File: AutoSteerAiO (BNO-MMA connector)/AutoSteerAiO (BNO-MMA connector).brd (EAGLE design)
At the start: 114.3 x 99.1 mm, 88 parts, among them J4 CONNECTOR 1x5 PINS, K4 CB1A-P-12V, T1 BC547, U1 VX7805-1000

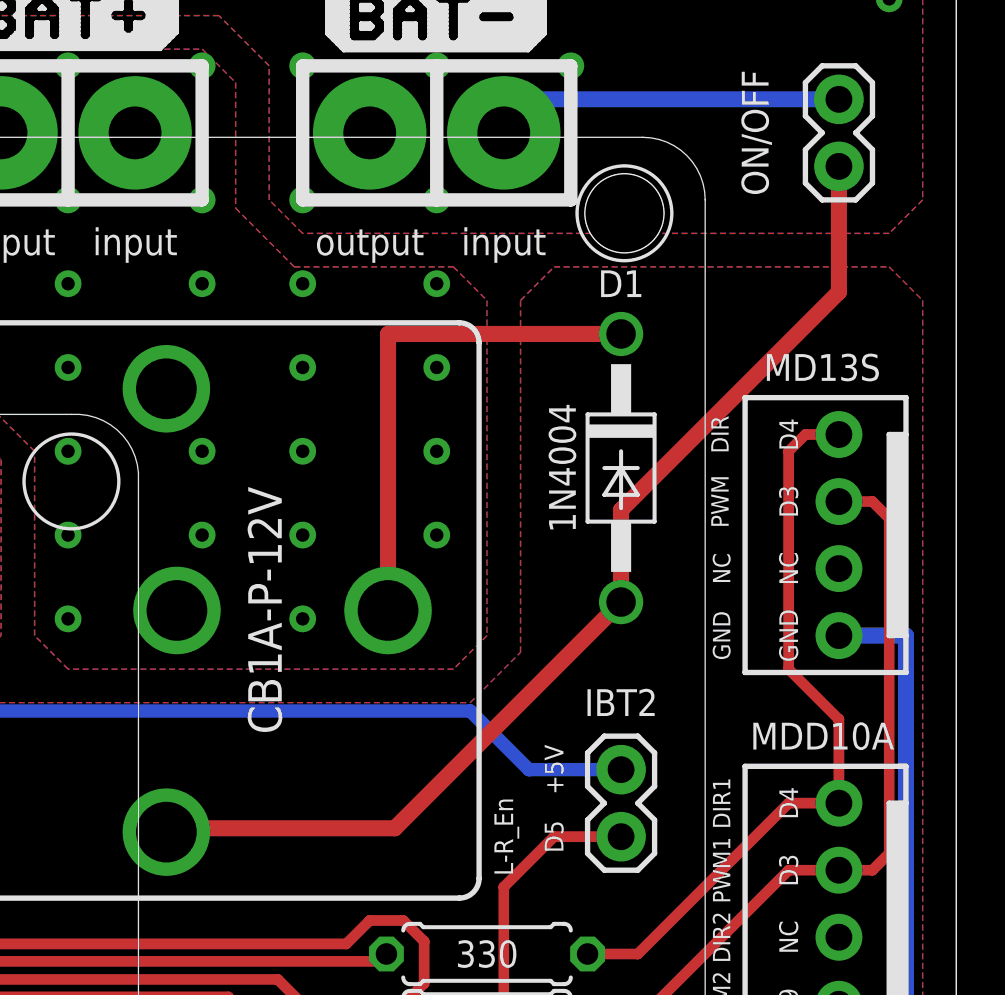
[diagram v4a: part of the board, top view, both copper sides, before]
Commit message: Add files via upload
Added diode D6 to protect from reverse polarity
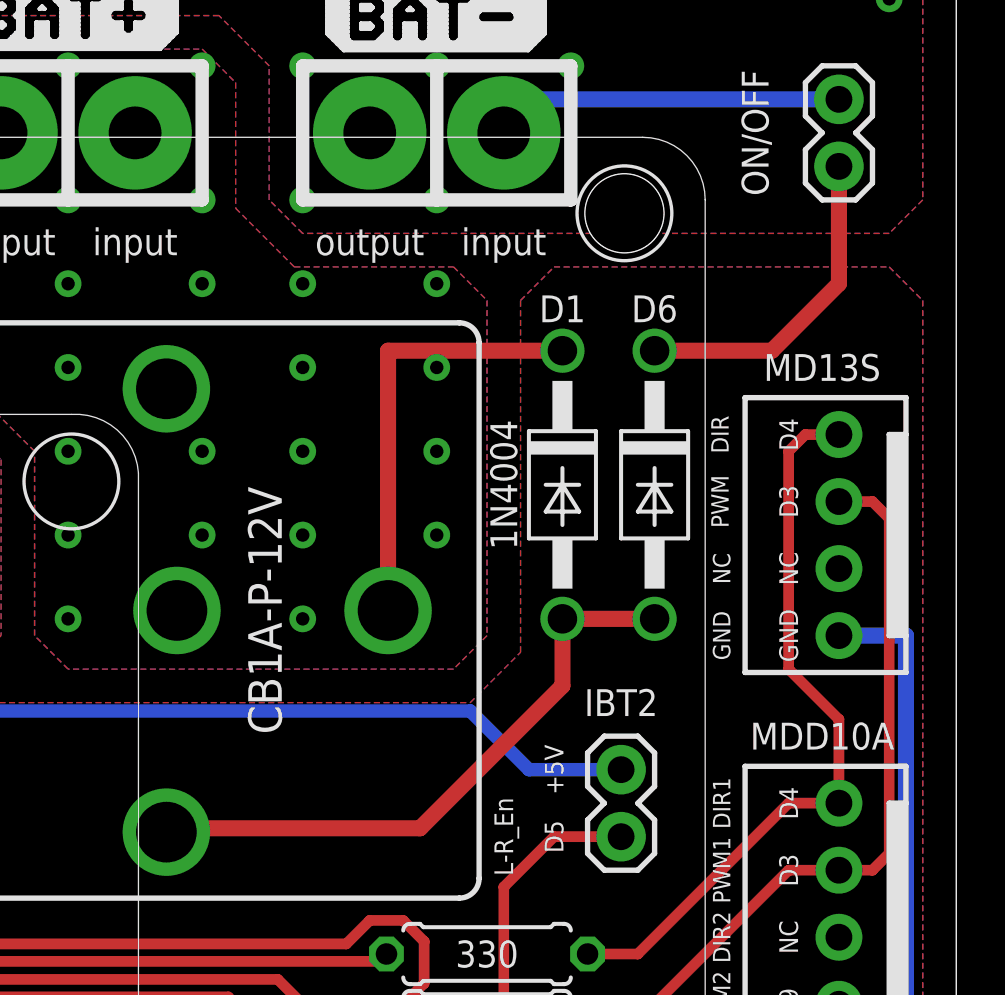
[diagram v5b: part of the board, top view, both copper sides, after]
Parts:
- added D6: 1N4004, diode:DO41-10
- moved D1 2.31 mm to (99.4, 71.8)
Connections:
- new net N$28: D6.C, ON/OFF.2
- net N$5: now also D6.A; no longer ON/OFF.2
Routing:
- net N$5: track 40.9 -> 23.4 mm
- net N$28: track 0.00 -> 12.5 mm
- net V+: track 19.3 -> 16.4 mm
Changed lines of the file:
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@@
 <attribute name="CYTRON-PC" value="CN-2600PS-05" x="109.855" y="49.53" size="1.778" layer="27" rot="R90" display="off"/>
 <attribute name="DESC" value="2600 PCB Connector" x="109.855" y="49.53" size="1.778" layer="27" rot="R90" display="off"/>
+<attribute name="LABEL" value="" x="112.776" y="48.133" size="0.762" layer="21" font="vector" ratio="15" rot="R90" align="top-left"/>
 <attribute name="LABEL" value="" x="112.776" y="48.133" size="0.762" layer="51" font="vector" ratio="15" rot="R90" align="top-left"/>
-<attribute name="LABEL" value="" x="112.776" y="48.133" size="0.762" layer="21" font="vector" ratio="15" rot="R90" align="top-left"/>
 <attribute name="LABEL" value="" x="109.855" y="49.53" size="1.778" layer="27" rot="R90" display="off"/>
 <attribute name="MF" value="" x="109.855" y="49.53" size="1.778" layer="27" rot="R90" display="off"/>
@@
 <attribute name="OC_NEWARK" value="unknown" x="45.847" y="3.302" size="1.778" layer="27" display="off"/>
 </element>
-<element name="D1" library="diode" library_urn="urn:adsk.eagle:library:210" package="DO41-10" package3d_urn="urn:adsk.eagle:package:43336/1" value="1N4004" x="101.6" y="72.39" smashed="yes" rot="R270">
-<attribute name="MF" value="" x="101.6" y="72.39" size="1.778" layer="27" rot="R270" display="off"/>
-<attribute name="MPN" value="" x="101.6" y="72.39" size="1.778" layer="27" rot="R270" display="off"/>
-<attribute name="NAME" x="101.6" y="79.375" size="1.016" layer="25" font="vector" ratio="12" align="center"/>
-<attribute name="OC_NEWARK" value="unknown" x="101.6" y="72.39" size="1.778" layer="27" rot="R270" display="off"/>
-<attribute name="VALUE" x="99.3775" y="72.39" size="1.016" layer="25" font="vector" ratio="12" rot="R270" align="center"/>
+<element name="D1" library="diode" library_urn="urn:adsk.eagle:library:210" package="DO41-10" package3d_urn="urn:adsk.eagle:package:43336/1" value="1N4004" x="99.3775" y="71.755" smashed="yes" rot="R270">
+<attribute name="MF" value="" x="99.3775" y="71.755" size="1.778" layer="27" rot="R270" display="off"/>
+<attribute name="MPN" value="" x="99.3775" y="71.755" size="1.778" layer="27" rot="R270" display="off"/>
+<attribute name="NAME" x="99.3775" y="78.4225" size="1.016" layer="25" font="vector" ratio="12" align="center"/>
+<attribute name="OC_NEWARK" value="unknown" x="99.3775" y="71.755" size="1.778" layer="27" rot="R270" display="off"/>
+<attribute name="VALUE" x="97.155" y="71.755" size="1.016" layer="25" font="vector" ratio="12" rot="R270" align="center"/>
 </element>
 <element name="C5" library="SparkFun-Capacitors" library_urn="urn:adsk.eagle:library:510" package="CPOL-RADIAL-5MM-10MM" package3d_urn="urn:adsk.eagle:package:37412/1" value="1000uF 35V" x="15.5575" y="93.0275" smashed="yes" rot="R270">
@@
 <attribute name="NAME" x="99.06" y="58.42" size="0.7112" layer="25" font="vector" ratio="15" rot="R270" align="center"/>
 <attribute name="OC_NEWARK" value="unknown" x="101.6" y="58.42" size="1.778" layer="27" rot="R90" display="off"/>
+</element>
+<element name="D6" library="diode" library_urn="urn:adsk.eagle:library:210" package="DO41-10" package3d_urn="urn:adsk.eagle:package:43336/1" value="1N4004" x="102.87" y="71.755" smashed="yes" rot="R270">
+<attribute name="MF" value="" x="102.87" y="71.755" size="1.778" layer="27" rot="R270" display="off"/>
+<attribute name="MPN" value="" x="102.87" y="71.755" size="1.778" layer="27" rot="R270" display="off"/>
+<attribute name="NAME" x="102.87" y="78.4225" size="1.016" layer="25" font="vector" ratio="12" align="center"/>
+<attribute name="OC_NEWARK" value="unknown" x="102.87" y="71.755" size="1.778" layer="27" rot="R270" display="off"/>
 </element>
 </elements>
@@
 <vertex x="96.52" y="78.74"/>
 </polygon>
-<wire x1="101.6" y1="77.47" x2="92.77" y2="77.47" width="0.6096" layer="1"/>
-<wire x1="92.77" y1="77.47" x2="92.77" y2="66.9925" width="0.6096" layer="1"/>
+<wire x1="99.3775" y1="76.835" x2="92.77" y2="76.835" width="0.6096" layer="1"/>
+<wire x1="92.77" y1="76.835" x2="92.77" y2="66.9925" width="0.6096" layer="1"/>
 <via x="94.615" y="73.025" extent="1-16" drill="0.508"/>
 <via x="80.645" y="76.2" extent="1-16" drill="0.508"/>
@@
 </signal>
 <signal name="N$5">
-<contactref element="ON/OFF" pad="2"/>
 <contactref element="K4" pad="86"/>
 <contactref element="D1" pad="A"/>
 <wire x1="84.37" y1="58.5925" x2="84.37" y2="58.7375" width="0.6096" layer="1"/>
-<wire x1="101.6" y1="67.31" x2="93.0275" y2="58.7375" width="0.6096" layer="1"/>
-<wire x1="93.0275" y1="58.7375" x2="84.37" y2="58.7375" width="0.6096" layer="1"/>
-<wire x1="101.6" y1="67.31" x2="101.6" y2="70.8025" width="0.6096" layer="1"/>
-<wire x1="101.6" y1="70.8025" x2="109.855" y2="79.0575" width="0.6096" layer="1"/>
-<wire x1="109.855" y1="79.0575" x2="109.855" y2="83.82" width="0.6096" layer="1"/>
+<wire x1="99.3775" y1="66.675" x2="99.3775" y2="64.135" width="0.6096" layer="1"/>
+<wire x1="99.3775" y1="64.135" x2="93.98" y2="58.7375" width="0.6096" layer="1"/>
+<wire x1="93.98" y1="58.7375" x2="84.37" y2="58.7375" width="0.6096" layer="1"/>
+<contactref element="D6" pad="A"/>
+<wire x1="102.87" y1="66.675" x2="99.3775" y2="66.675" width="0.6096" layer="1"/>
 </signal>
 <signal name="N$2">
@@
 <wire x1="91.44" y1="44.45" x2="93.98" y2="44.45" width="0.4064" layer="1"/>
 </signal>
+<signal name="N$28">
+<contactref element="ON/OFF" pad="2"/>
+<contactref element="D6" pad="C"/>
+<wire x1="102.87" y1="76.835" x2="107.315" y2="76.835" width="0.6096" layer="1"/>
+<wire x1="107.315" y1="76.835" x2="109.855" y2="79.375" width="0.6096" layer="1"/>
+<wire x1="109.855" y1="79.375" x2="109.855" y2="83.82" width="0.6096" layer="1"/>
+</signal>
 </signals>
